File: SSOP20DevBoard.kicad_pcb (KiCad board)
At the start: 2 copper layers, 20 x 16 mm, 3 parts, among them J1 Conn_01x10_Male, J2 Conn_01x10_Male

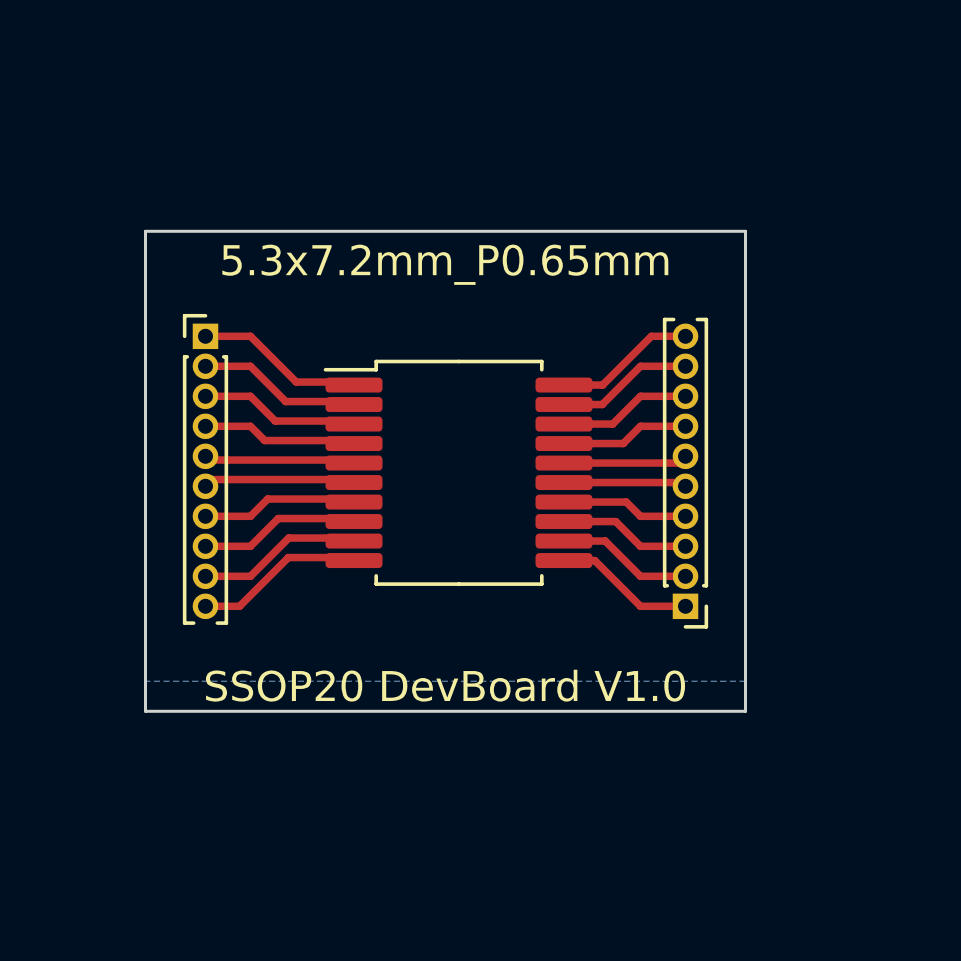
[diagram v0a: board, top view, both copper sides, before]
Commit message: changed pin connectors to correct size
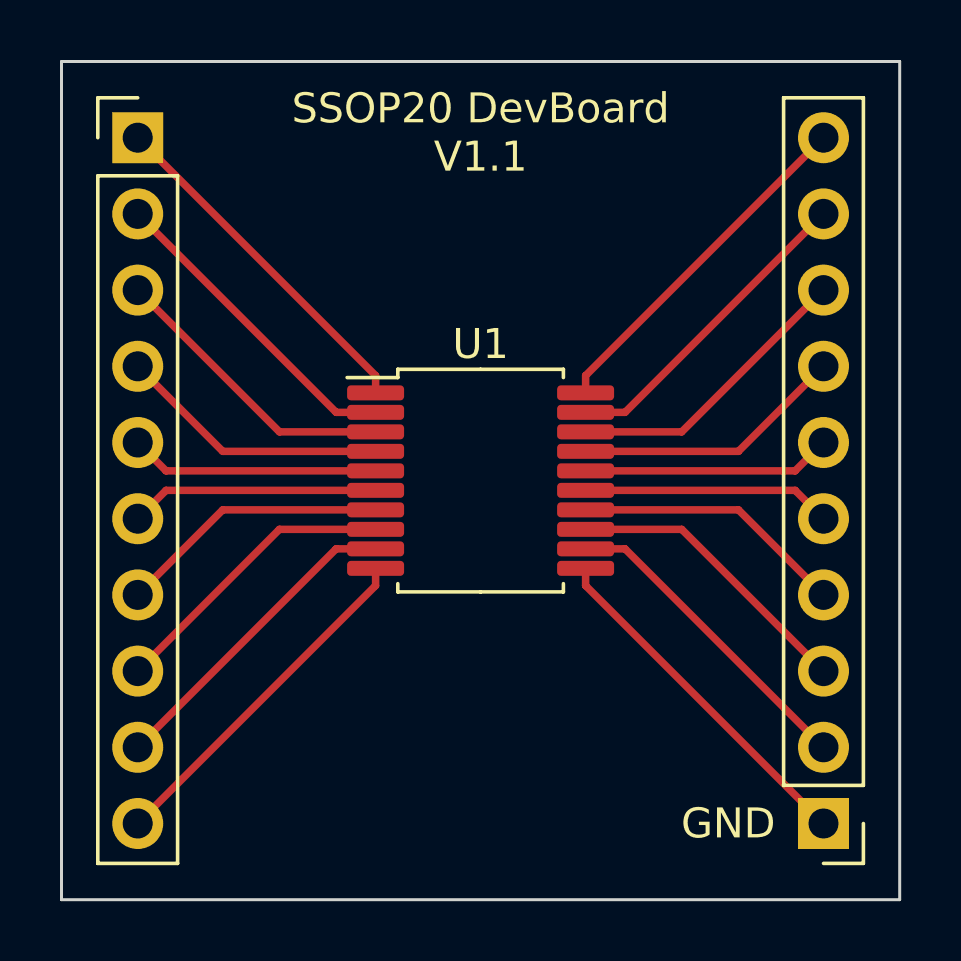
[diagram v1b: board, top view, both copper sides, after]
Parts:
- removed 5.3x7.2mm_P0.65mm: AD, Package_SO:SSOP-20_5.3x7.2mm_P0.65mm
- added U1: AD, Package_SO:SSOP-20_5.3x7.2mm_P0.65mm, F.Cu at (90.2, 67.3)
- J1, J2: footprint Connector_PinHeader_1.00mm:PinHeader_1x10_P1.00mm_Vertical -> Connector_PinHeader_2.54mm:PinHeader_1x10_P2.54mm_Vertical
- moved J2 8.58 mm to (101.6, 78.7)
- moved J1 7.00 mm to (78.7, 55.9)
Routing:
- net Net-(J1-Pad1): track 4.68 -> 11.8 mm
- net Net-(J2-Pad1): track 4.68 -> 11.8 mm
- net Net-(J1-Pad10): track 4.72 -> 11.8 mm
- net Net-(J2-Pad10): track 4.72 -> 11.8 mm
- net Net-(J2-Pad2): track 4.54 -> 10.7 mm
- net Net-(J1-Pad2): track 4.54 -> 10.7 mm
- net Net-(J1-Pad9): track 4.58 -> 10.7 mm
- net Net-(J2-Pad9): track 4.58 -> 10.7 mm
- net Net-(J1-Pad3): track 4.39 -> 9.89 mm
- net Net-(J2-Pad3): track 4.39 -> 9.89 mm
- net Net-(J1-Pad8): track 4.43 -> 9.89 mm
- net Net-(J2-Pad8): track 4.43 -> 9.89 mm
- net Net-(J2-Pad4): track 4.25 -> 9.10 mm
- net Net-(J1-Pad4): track 4.25 -> 9.10 mm
- net Net-(J1-Pad7): track 4.29 -> 9.10 mm
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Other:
- board size 20 x 16 mm -> 27.9 x 27.9 mm
- board text added: "GND"
- board text added: "SSOP20 DevBoard V1.1"
- board text removed: "SSOP20 DevBoard V1.0"
